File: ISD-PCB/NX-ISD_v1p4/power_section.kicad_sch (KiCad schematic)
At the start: 30 parts, among them J1 UJ20-C-H-G-SMT-1-P16-TR, P1 S2B-PH-SM4-TB, Q1 BC847W, Q2 AO3401A, U1 RT9193-18GB, U2 USBLC6-2P6, U3 TLV62568DBV, U5 BQ25170DSGR

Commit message: hw(v1.4): progress on TODO - 4-bit MicroSD, direct display bus, BNO085 & EP vias (DRC 0 errors)
- Implemented 4-bit SDMMC MicroSD slot (Molex 105162-0001) on right edge with outward insertion
- Routed direct 3.3V display SPI bus (TE 1-2328702-0) with C29 100nF decoupling
- Centered BNO085 9-DOF IMU cluster with local ground star and 32.768kHz crystal
- Rerouted NeoPixel PWR_NPM high-side power gate signal
- Updated thermal EP pad via sizes on BQ25170 and MAX17048 for standard JLCPCB fabrication
- Achieved 0 DRC errors, 0 unconnected nets, and 100% schematic parity
- Updated HW-TODO and SW-TODO for v1.3/v1.4 pinout target abstraction
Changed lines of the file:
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@@
 	(wire
 		(pts
-			(xy 83.82 45.72) (xy 86.36 45.72)
+			(xy 83.82 45.72) (xy 96.52 45.72)
 		)
 		(stroke
@@
 	(wire
 		(pts
-			(xy 83.82 48.26) (xy 86.36 48.26)
+			(xy 83.82 48.26) (xy 96.52 48.26)
 		)
 		(stroke
@@
 	(hierarchical_label "D+"
 		(shape bidirectional)
-		(at 86.36 45.72 0)
+		(at 96.52 45.72 0)
 		(effects
 			(font
@@
 	(hierarchical_label "D-"
 		(shape bidirectional)
-		(at 86.36 48.26 0)
-		(effects
-			(font
+		(at 96.52 48.26 0)
+		(effects
+			(font

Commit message: hw(v1.4): bq25170 thermal optimization, usb-c plating, battery pad stitching, and npm decoupling
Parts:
- R6: value 499 -> 604
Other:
- note added: "604 Ω / ~500 mA"
- note removed: "500 Ω / 600 mA"
- note removed: "IF NOT SPECIFID IN [0x0x] THEN ALL PASSIVE PARTS ARE IN: [0402]"
- title: (none) -> NX-ISD Version 1 Rev. 4
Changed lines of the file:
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@@
 	(generator_version "10.0")
 	(paper "A4")
+	(title_block
+		(title "NX-ISD Version 1 Rev. 4")
+		(date "2026-10-16")
+		(rev "p4")
+		(comment 1 "IF NOT SPECIFID IN [0x0x] THEN ALL PASSIVE PARTS ARE IN: [0402]")
+	)
 	(rectangle
 		(start 138.176 123.19)
@@
 		)
 	)
-	(text "IF NOT SPECIFID IN [0x0x] THEN ALL PASSIVE PARTS ARE IN: [0402]"
-		(exclude_from_sim no)
-		(at 210.82 168.91 0)
-		(effects
-			(font
-				(size 1.27 1.27)
-			)
-		)
-	)
 	(text "[0603]"
 		(exclude_from_sim no)
@@
 		)
 	)
-	(text "500 Ω / 600 mA"
+	(text "604 Ω / ~500 mA"
 		(exclude_from_sim no)
 		(at 215.392 69.088 0)
@@
 			)
 		)
-		(property "Value" "499"
+		(property "Value" "604"
 			(at 201.93 66.548 90)
 			(show_name no)

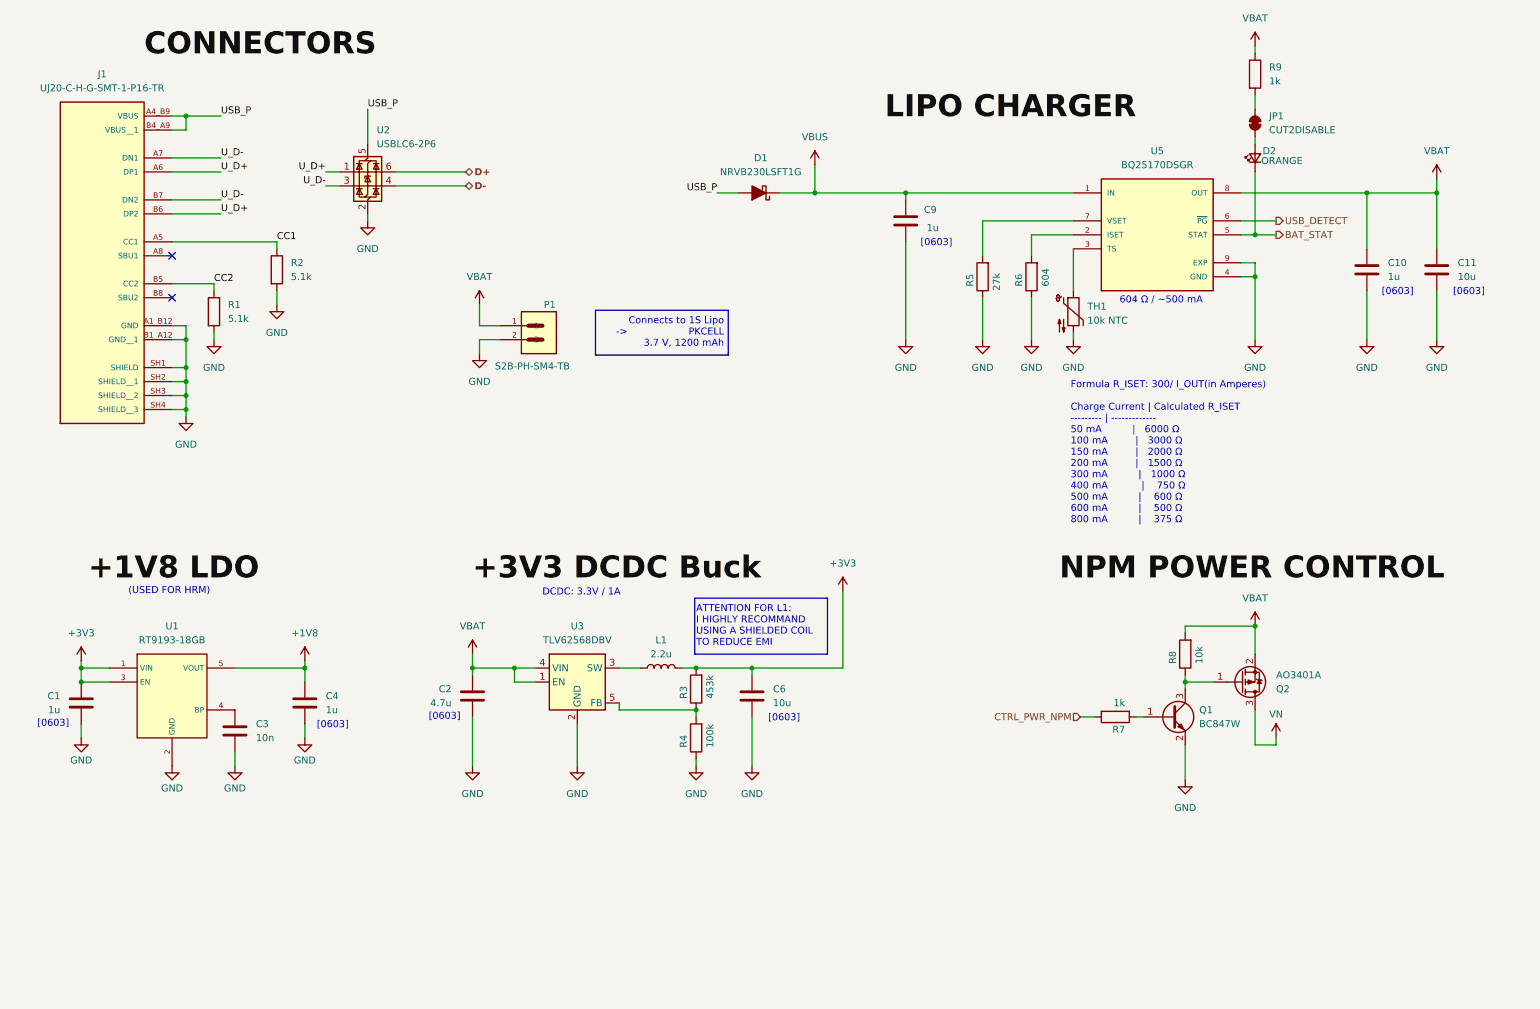
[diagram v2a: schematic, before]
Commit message: hw(v1.4): complete overall layout plating, esp32 thermal pad, npm silkscreen, and docs
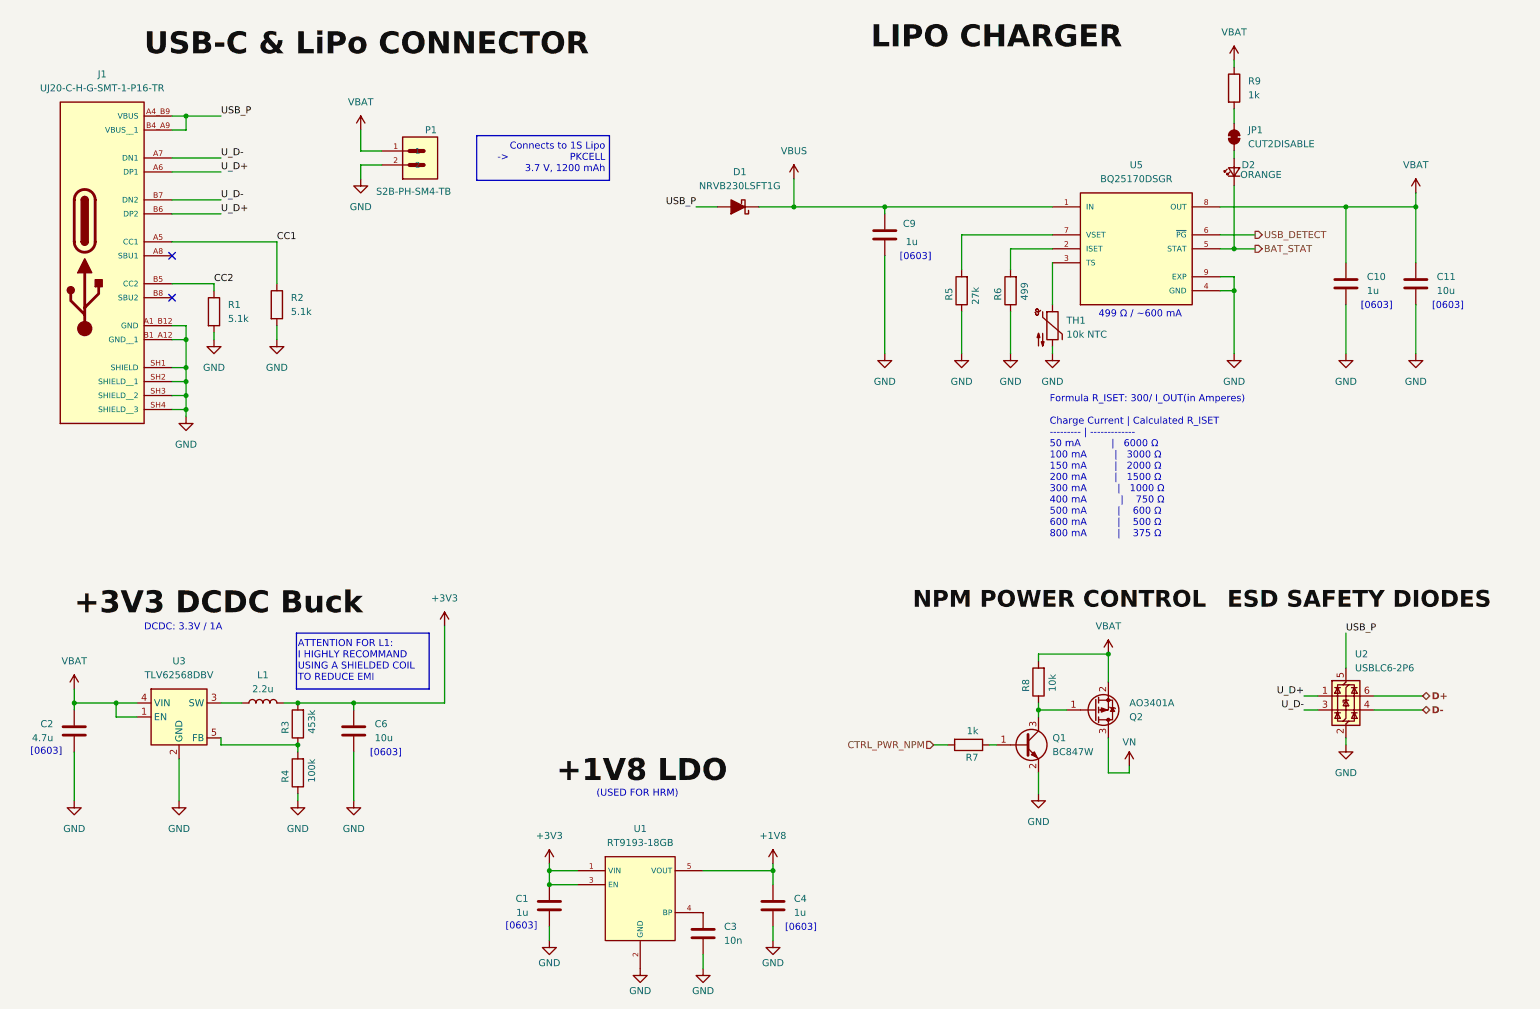
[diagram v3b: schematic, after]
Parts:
- R6: value 604 -> 499
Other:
- note added: "499 Ω / ~600 mA"
- note removed: "604 Ω / ~500 mA"
- moved on the sheet: C1, C10, C11, C2, C3, C4, C6, C9, D1, D2, JP1, L1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
